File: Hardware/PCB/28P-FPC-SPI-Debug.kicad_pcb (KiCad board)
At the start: 2 copper layers, 97.4 x 36.8 mm, 35 parts, among them J1 Conn_01x08, J2 Conn_01x24, J3 SFV24R-1STBE1HLF, Q1 Si1308EDL, Q2 AO3401A, Q3 S8050, U1 RT9193-33GB, U2 TXB0108PW

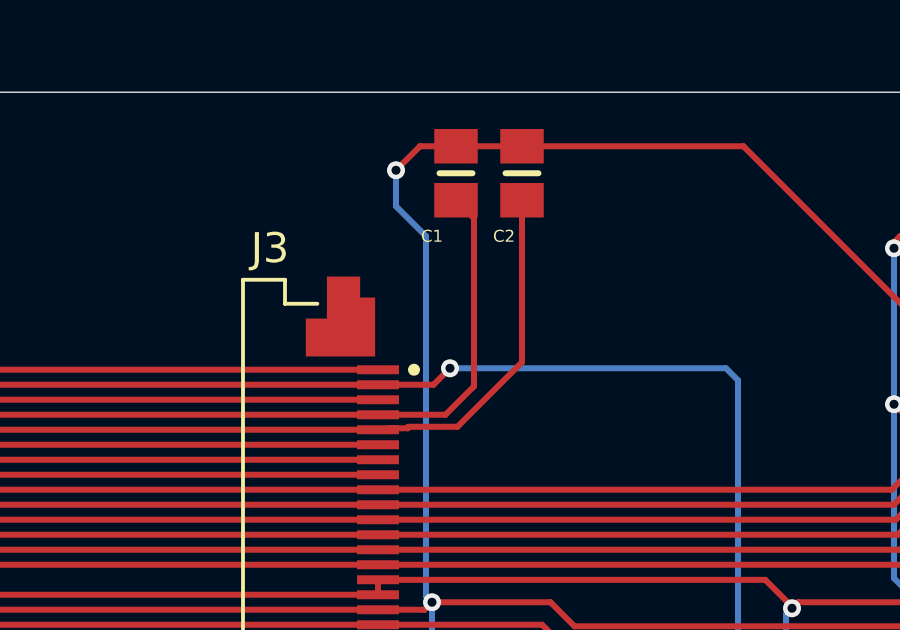
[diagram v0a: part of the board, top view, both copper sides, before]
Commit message: Added STM32 NUCLEO-L433RC project with basic pin assignments to J1 jumper on PCB for project start. Modified folder structure.
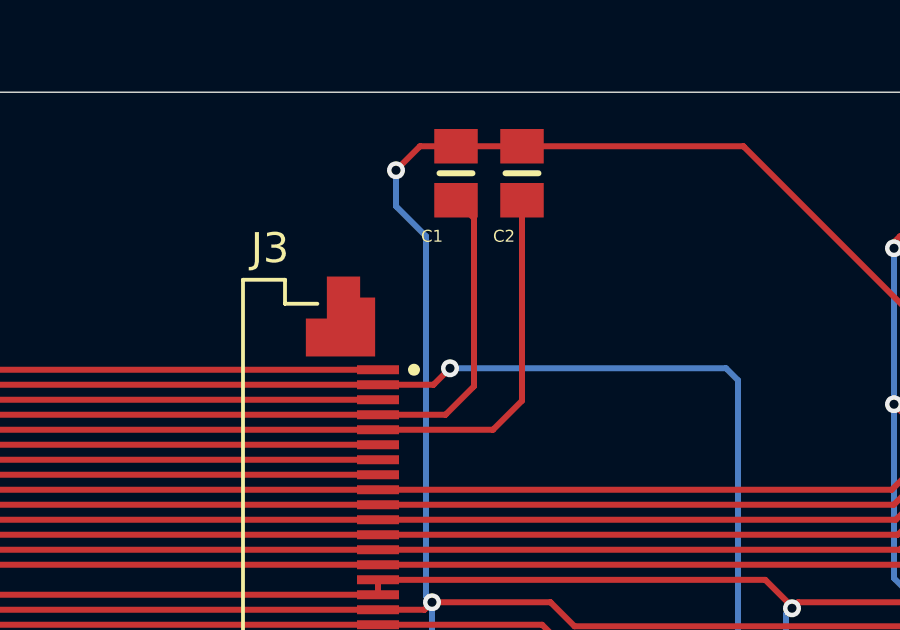
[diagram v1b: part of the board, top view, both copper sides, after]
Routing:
- net /VGH: track 48.7 -> 49.4 mm
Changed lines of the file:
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@@
 			(plot_on_all_layers_selection 0x00000000_00000000_00000000_00000000)
 			(disableapertmacros no)
-			(usegerberextensions no)
+			(usegerberextensions yes)
 			(usegerberattributes yes)
 			(usegerberadvancedattributes yes)
-			(creategerberjobfile yes)
+			(creategerberjobfile no)
 			(dashed_line_dash_ratio 12.000000)
 			(dashed_line_gap_ratio 3.000000)
@@
 			(sketchdnponfab yes)
 			(crossoutdnponfab yes)
-			(subtractmaskfromsilk no)
+			(subtractmaskfromsilk yes)
 			(outputformat 1)
 			(mirror no)
-			(drillshape 1)
+			(drillshape 0)
 			(scaleselection 1)
-			(outputdirectory "")
+			(outputdirectory "./")
 		)
 	)
@@
 	)
 	(segment
-		(start 148.401 56.151)
-		(end 150.049 56.151)
-		(width 0.2)
-		(layer "F.Cu")
-		(net 8)
-	)
-	(segment
-		(start 150.049 56.151)
-		(end 152.2 54)
-		(width 0.2)
-		(layer "F.Cu")
-		(net 8)
-	)
-	(segment
-		(start 152.2 54)
-		(end 152.2 48.6)
-		(width 0.2)
-		(layer "F.Cu")
-		(net 8)
-	)
-	(segment
 		(start 147.4 56.25)
-		(end 147.75 56.25)
-		(width 0.2)
-		(layer "F.Cu")
-		(net 8)
-	)
-	(segment
-		(start 147.75 56.25)
-		(end 147.799 56.201)
+		(end 151.23355 56.25)
 		(width 0.2)
 		(layer "F.Cu")
@@
 	)
 	(segment
-		(start 148.401 56.201)
-		(end 148.401 56.151)
+		(start 152.2 55.28355)
+		(end 152.2 48.6)
 		(width 0.2)
 		(layer "F.Cu")
@@
 	)
 	(segment
-		(start 147.799 56.201)
-		(end 148.401 56.201)
+		(start 151.23355 56.25)
+		(end 152.2 55.28355)
 		(width 0.2)
 		(layer "F.Cu")

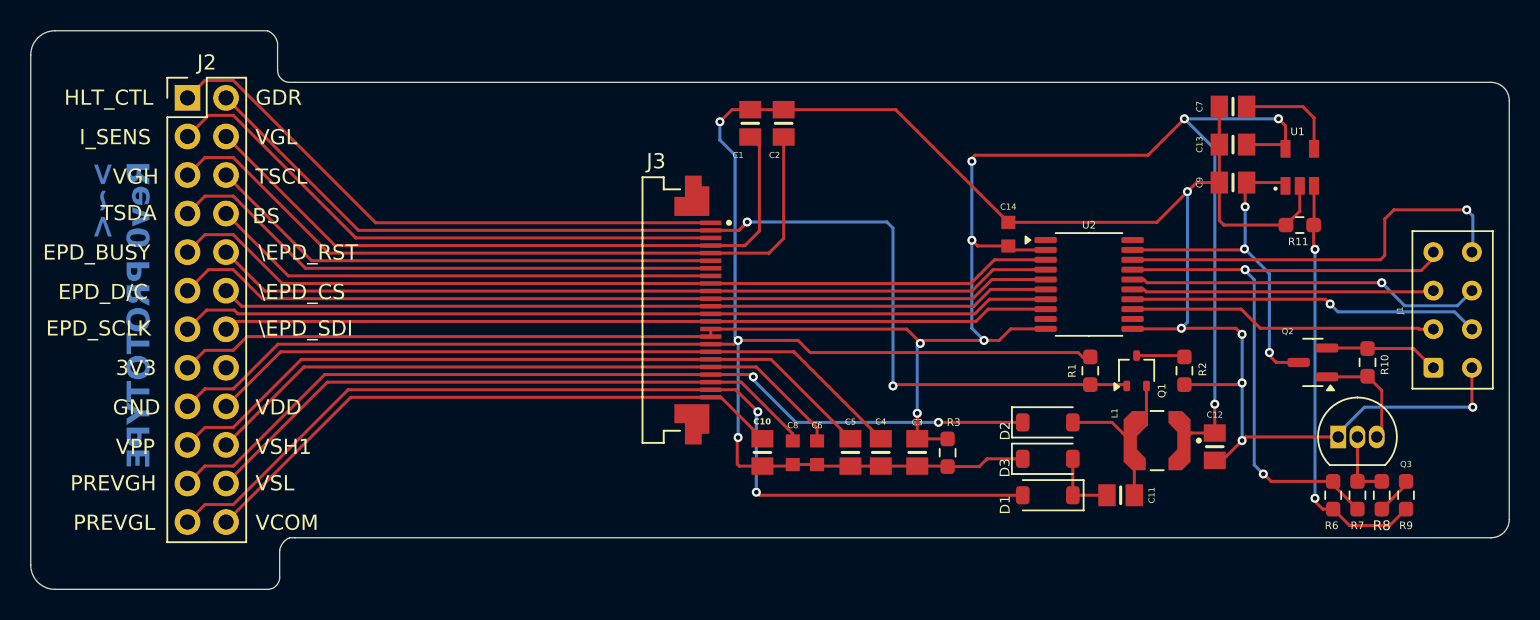
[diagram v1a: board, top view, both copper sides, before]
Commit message: Modified J1 footprint to 1.7mm through hole. Added copper pours and GND via stitching for thermal relief. Plus some other stuff I can't remember. E-paper waveshare libs added to STM32 project. Project configuration via MXCube, pin assignment, clock configuration. Basic framework setup for testing.
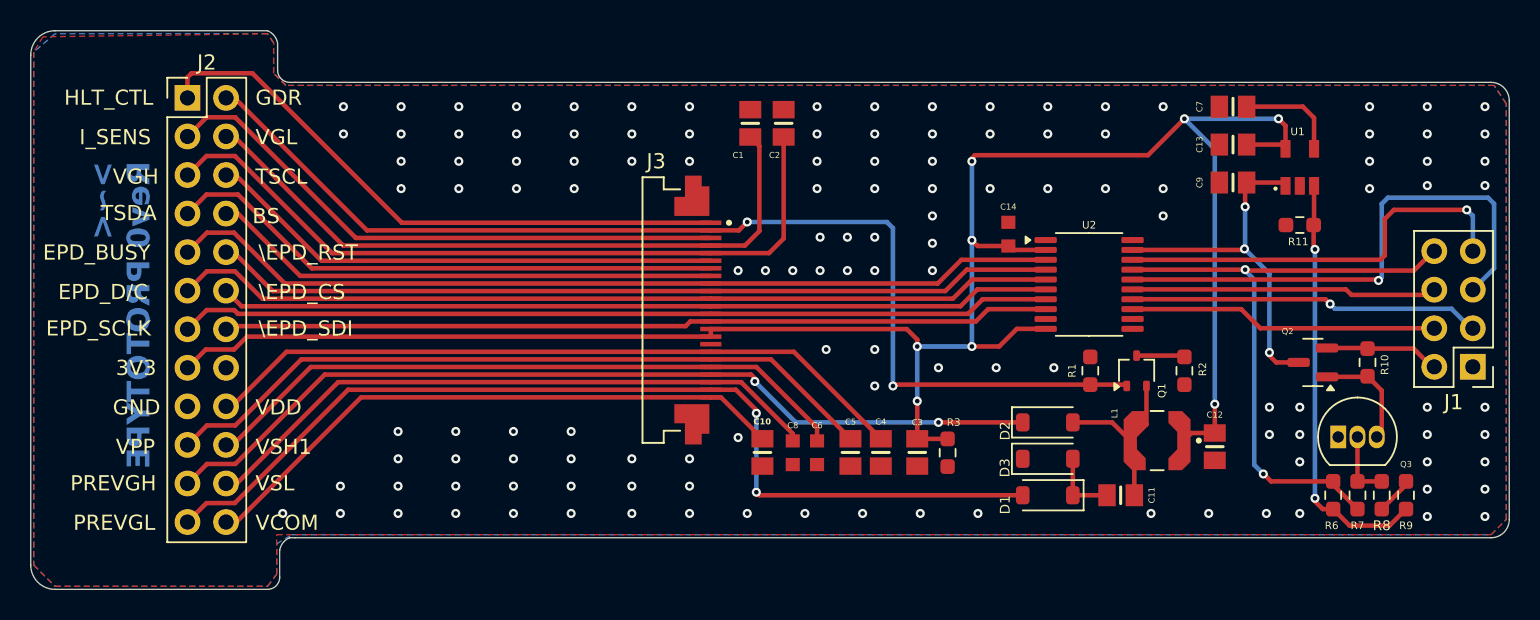
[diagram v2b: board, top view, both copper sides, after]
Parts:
- J1: footprint Connector_Samtec_HLE_THT:Samtec_HLE-104-02-xx-DV-TE_2x04_P2.54mm_Horizontal -> Connector_PinHeader_2.54mm:PinHeader_2x04_P2.54mm_Vertical
- moved J1 2.60 mm to (197.6, 63.7), turned to 180 degrees
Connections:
- J1 pad 1: /VCC_INT -> GND
- J1 pad 2: GND -> /VCC_INT
- J1 pad 3: /SDI -> /SCLK
- J1 pad 4: /SCLK -> /SDI
- J1 pad 5: /CS -> /D/C
- J1 pad 6: /D/C -> /CS
- J1 pad 7: /\RST -> /BUSY
- J1 pad 8: /BUSY -> /\RST
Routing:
- net GND: track 204.9 -> 0.00 mm, vias 9 -> 128
- net /D/C: track 23.5 -> 35.3 mm
- net /HLT_CTL: track 38.8 -> 40.0 mm
- added copper zone on B.Cu, net GND
- added copper zone on F.Cu, net GND

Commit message: Mirror pins on FPC connector. Reposition components. Copper pours
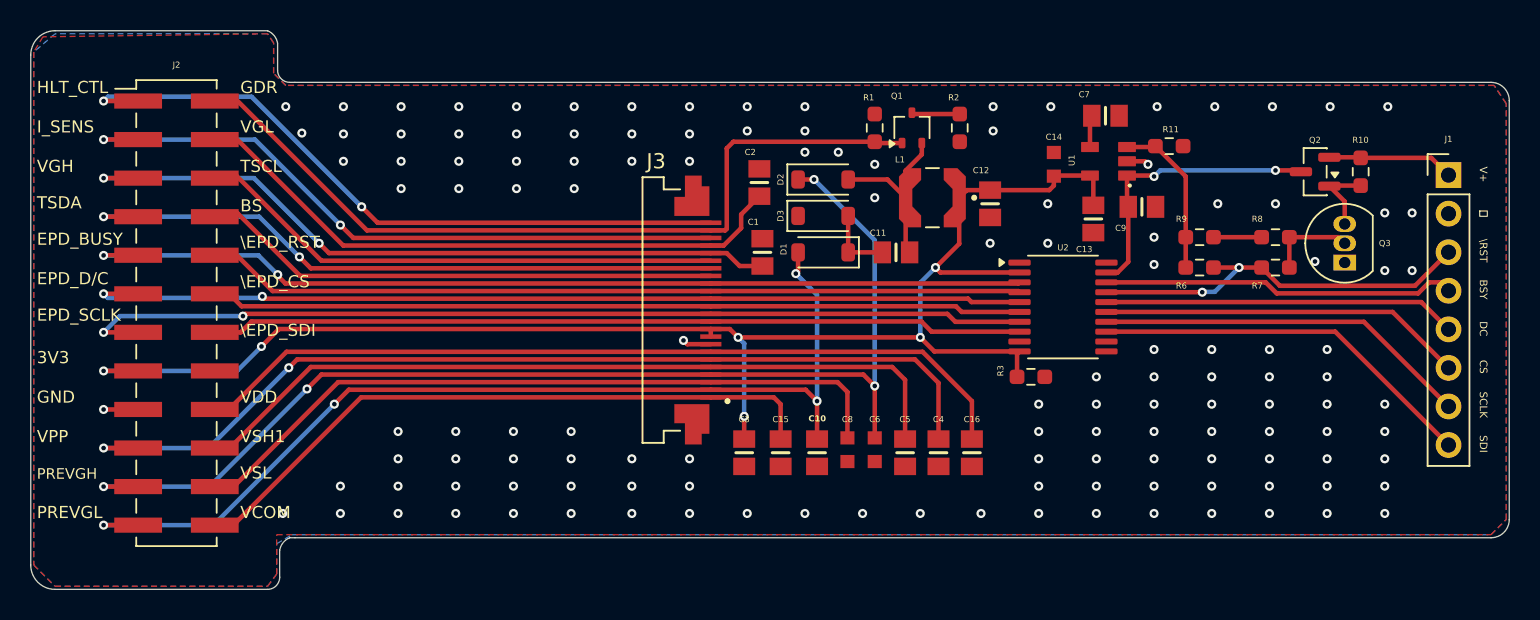
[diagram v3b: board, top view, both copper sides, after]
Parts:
- added C15: 1u/50V, capacitors-cam:CAPC2012X140N, F.Cu at (152.0, 69.4)
- added C16: 1u/50V, capacitors-cam:CAPC2012X140N, F.Cu at (164.6, 69.4)
- J1: footprint Connector_PinHeader_2.54mm:PinHeader_2x04_P2.54mm_Vertical -> Connector_PinHeader_2.54mm:PinHeader_1x08_P2.54mm_Vertical
- J2: footprint Connector_PinHeader_2.54mm:PinHeader_2x12_P2.54mm_Vertical -> Connector_PinHeader_2.54mm:PinHeader_2x12_P2.54mm_Vertical_SMD
- moved C11 21.8 mm to (159.6, 56.2)
- moved L1 21.8 mm to (162.0, 52.6)
- moved D2 21.8 mm to (154.8, 51.4)
- moved C12 21.8 mm to (165.8, 53.0)
- moved D1 21.8 mm to (154.8, 56.2)
- moved D3 21.8 mm to (154.8, 53.8)
- moved Q1 21.8 mm to (160.7, 48.0)
- moved R2 21.8 mm to (163.8, 48.0)
- moved R9 21.8 mm to (179.6, 55.2), turned to 0 degrees
- moved R1 21.4 mm to (158.2, 48.0)
- moved R8 18.4 mm to (184.6, 55.2), turned to 0 degrees
- moved R6 17.4 mm to (179.6, 57.2), turned to 180 degrees
- moved R7 15.9 mm to (184.6, 57.2), turned to 180 degrees
- moved J2 14.2 mm to (112.2, 60.2)
- moved J1 12.7 mm to (196.0, 51.1), turned to 0 degrees
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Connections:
- C1 pad 2: /VGL -> /VGH
- C10 pad 1: GND -> /PREVGL
- C10 pad 2: /VCOM -> GND
- C2 pad 2: /VGH -> /VGL
- C4 pad 2: /VDD -> /VPP
- C5 pad 1: GND -> /VSH1
- C5 pad 2: /VPP -> GND
- C6 pad 1: GND -> /PREVGH
- C6 pad 2: /VSH1 -> GND
- C8 pad 1: GND -> /VSL
- C8 pad 2: /VSL -> GND
- J1 pad 1: GND -> /VCC_INT
- J1 pad 2: /VCC_INT -> GND
- J1 pad 3: /SCLK -> /\RST
- J1 pad 4: /SDI -> /BUSY
- J1 pad 7: /BUSY -> /SCLK
- J1 pad 8: /\RST -> /SDI
- J3 pad 1: /HLT_CTL -> /VCOM
- J3 pad 10: /\EPD_RST -> +3V3
- J3 pad 11: /EPD_D/C -> /EPD_SDI
- J3 pad 12: /EPD_CS -> /EPD_SCLK
- J3 pad 13: /EPD_SCLK -> /EPD_CS
- J3 pad 14: /EPD_SDI -> /EPD_D/C
- J3 pad 15: +3V3 -> /\EPD_RST
- J3 pad 16: +3V3 -> /EPD_BUSY
- J3 pad 17: GND -> /BS
- J3 pad 18: /VDD -> /TSDA
- J3 pad 19: /VPP -> /TSCL
- J3 pad 2: /GDR -> /PREVGL
- J3 pad 20: /VSH1 -> /VGH
- J3 pad 21: /PREVGH -> /VGL
- J3 pad 22: /VSL -> /CURR_SENSE
- J3 pad 23: /PREVGL -> /GDR
- J3 pad 24: /VCOM -> /HLT_CTL
- J3 pad 3: /CURR_SENSE -> /VSL
- J3 pad 4: /VGL -> /PREVGH
- J3 pad 5: /VGH -> /VSH1
- J3 pad 6: /TSCL -> /VPP
- J3 pad 7: /TSDA -> /VDD
- J3 pad 8: /BS -> GND
- J3 pad 9: /EPD_BUSY -> +3V3
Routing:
- net +3V3: track 134.4 -> 101.0 mm, vias 8 -> 6
- net /GDR: track 73.8 -> 53.7 mm, vias 2 -> 0
- net /PREVGH: track 59.4 -> 76.2 mm, vias 2 -> 4
- net /VCC_EN: track 27.5 -> 10.7 mm, vias 2 -> 0
- net /VPP: track 48.2 -> 64.0 mm, vias 0 -> 2
- net /\RST: track 41.6 -> 26.3 mm
- net /D/C: track 35.3 -> 23.3 mm, vias 1 -> 0
- net /VSH1: track 43.4 -> 51.1 mm
- net /VDD: track 47.0 -> 54.5 mm
- net /TSDA: track 37.0 -> 43.7 mm, vias 0 -> 2
- net /CURR_SENSE: track 38.3 -> 45.0 mm, vias 0 -> 2
- net /HLT_CTL: track 40.0 -> 45.8 mm, vias 0 -> 2
- net /EPD_SCLK: track 57.6 -> 63.3 mm, vias 0 -> 2
- net GND: track 0.00 -> 5.64 mm, vias 128 -> 132
- net /SDI: track 20.4 -> 25.6 mm
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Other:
- board text added: ">~< Rev1 PROTOTYPE"
- board text added: "BSY"
- board text added: "CS"
- board text added: "DC"
- board text added: "SCLK"
- board text added: "SDI"
- board text added: "V+"
- board text added: "\RST"
- board text added: "⏚"
- board text removed: ">~< Rev0 PROTOTYPE"

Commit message: Modified J3 FPC connector to top bottom connector FFC2B28-24-G.
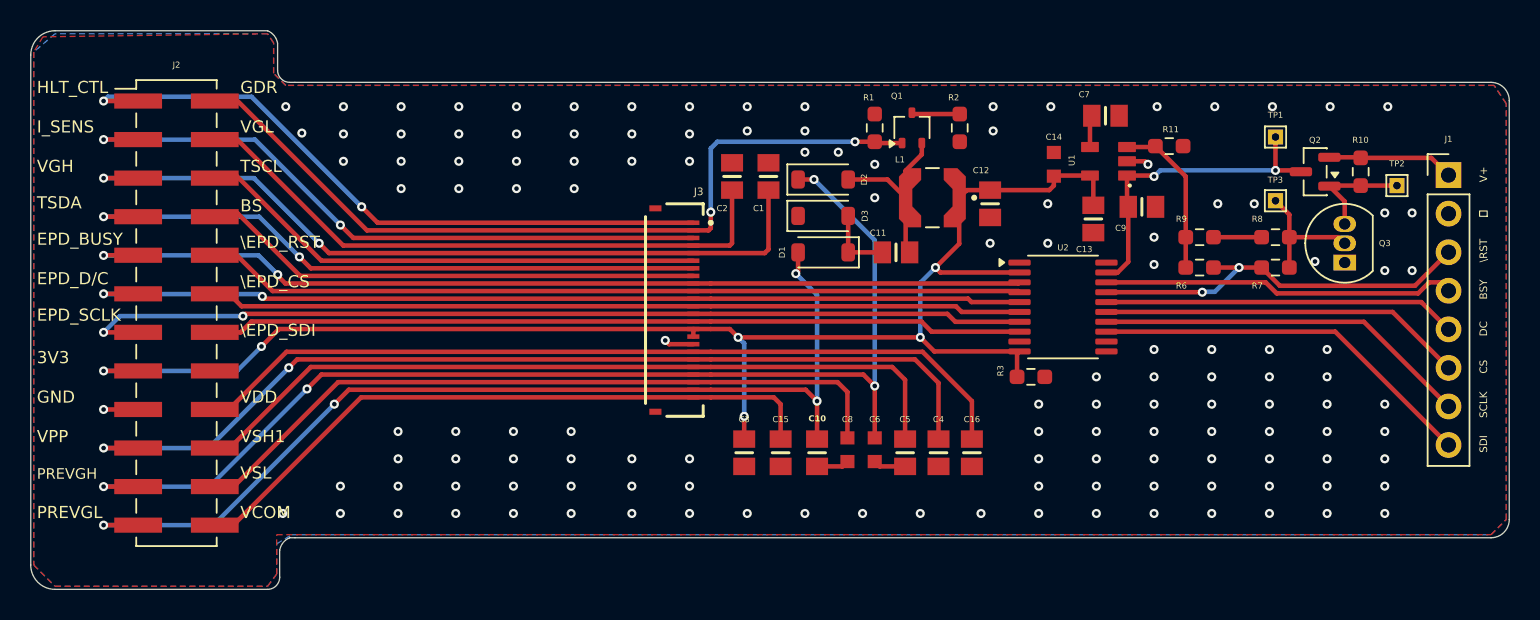
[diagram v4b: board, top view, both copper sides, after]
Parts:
- added TP1: ~, TestPoint:TestPoint_THTPad_1.0x1.0mm_Drill0.5mm, F.Cu at (184.6, 48.6)
- added TP2: ~, TestPoint:TestPoint_THTPad_1.0x1.0mm_Drill0.5mm, F.Cu at (192.6, 51.8)
- added TP3: ~, TestPoint:TestPoint_THTPad_1.0x1.0mm_Drill0.5mm, F.Cu at (184.6, 52.8)
- J3: value SFV24R-1STBE1HLF -> FFC2B28-24-G; footprint Connectors-cam:AMPHENOL_SFV24R-1STBE1HLF -> Connectors-cam:GCT_FFC2B28-24-G-1x24
- moved C1 5.02 mm to (151.2, 51.2)
- moved C2 1.84 mm to (148.8, 51.2)
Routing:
- net GND: track 5.64 -> 9.96 mm
- net /VGH: track 48.1 -> 52.1 mm
- net Net-(Q3-B): track 5.81 -> 8.59 mm
- net Net-(Q2-G): track 4.99 -> 7.38 mm
- net /Vcc: track 19.1 -> 21.3 mm
- net /TSDA: track 43.7 -> 42.5 mm
- net /TSCL: track 34.3 -> 33.1 mm
- net /HLT_CTL: track 45.8 -> 44.7 mm
- net /CURR_SENSE: track 45.0 -> 43.8 mm
- net /BS: track 33.6 -> 32.5 mm
- net /GDR: vias 0 -> 2
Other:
- board text added: "₍ ^. .^₎ Rev1.1 PROTOTYPE"
- board text removed: ">~< Rev1 PROTOTYPE"

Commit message: Modified FPC capacitor footprints to 0603 and 0805 due to production issues.
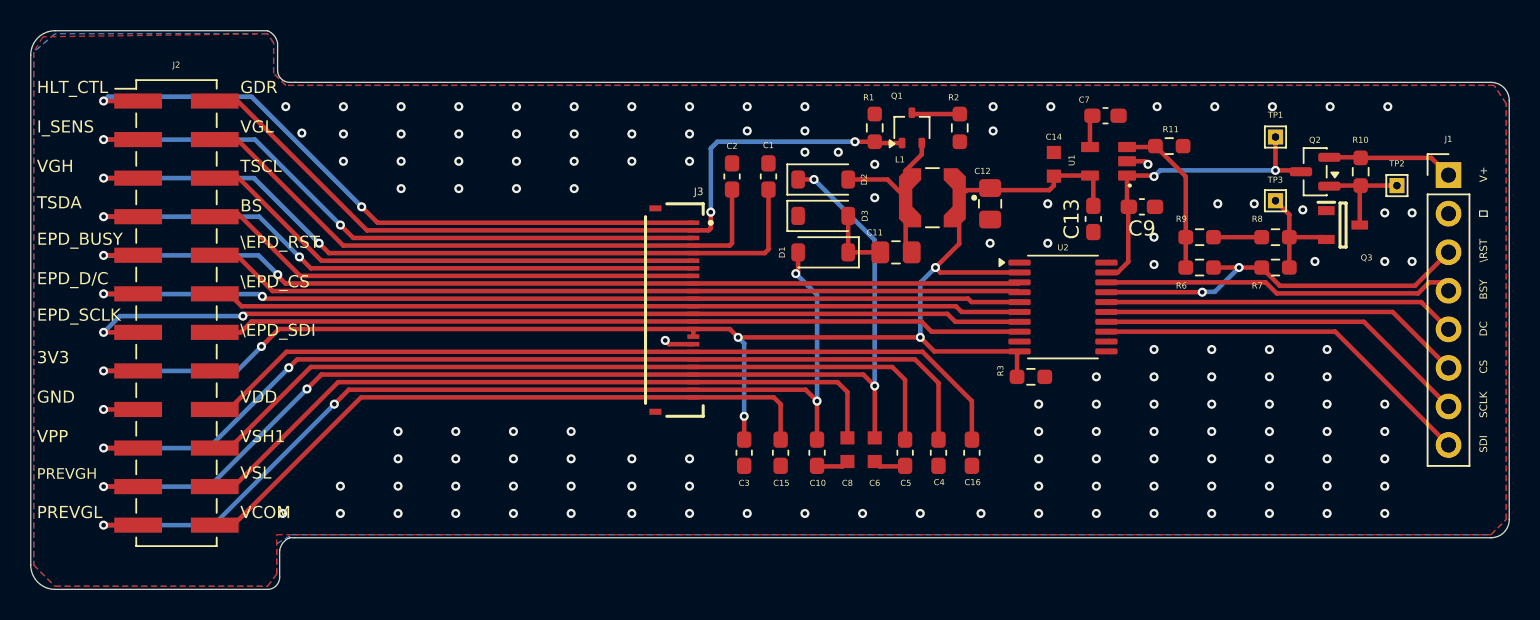
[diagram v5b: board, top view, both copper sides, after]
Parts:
- C1, C10, C13, C15, C16, C2, C3, C4, C5, C7, C9: footprint capacitors-cam:CAPC2012X140N -> Capacitor_SMD:C_0603_1608Metric_Pad1.08x0.95mm_HandSolder
- C11, C12: footprint capacitors-cam:CAPC2012X140N -> Capacitor_SMD:C_0805_2012Metric_Pad1.18x1.45mm_HandSolder
- J3: value FFC2B28-24-G -> SFV24R-1STBE1HLF
- Q3: footprint Package_TO_SOT_THT:TO-92_Inline -> mosfets:S8050
- moved Q3 2.47 mm to (189.1, 54.4), turned to 0 degrees
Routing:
- net Net-(Q3-B): track 8.59 -> 7.07 mm
- net /GDR: track 53.7 -> 53.0 mm
- net /VCOM: track 42.4 -> 41.7 mm
- net /TSCL: track 33.1 -> 32.5 mm
- net /VGL: track 39.9 -> 39.3 mm
- net /\EPD_RST: track 53.4 -> 52.9 mm
- net GND: vias 132 -> 133
